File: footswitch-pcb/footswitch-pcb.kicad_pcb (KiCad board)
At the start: 2 copper layers, 56 x 22 mm, 18 parts, among them Q1 BUK7880-55A, U1 SeeeduinoXIAO

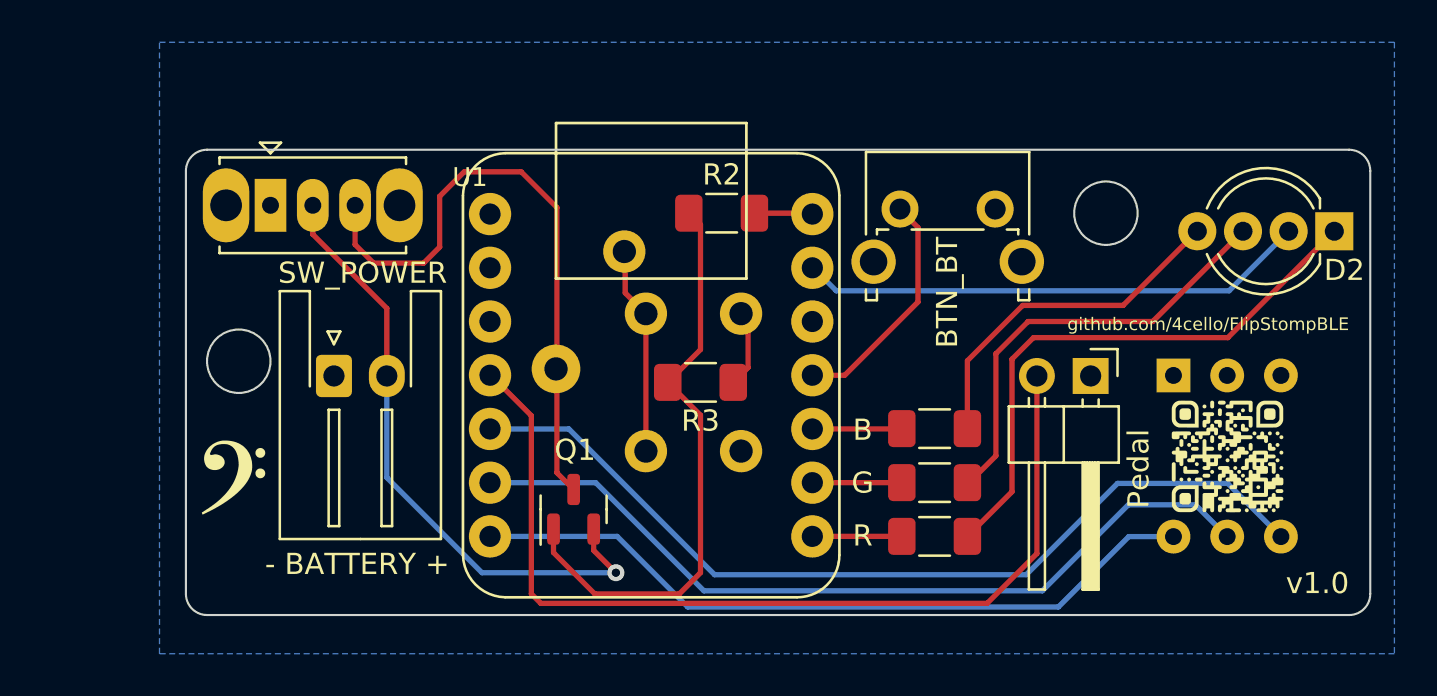
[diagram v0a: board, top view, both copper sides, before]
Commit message: Onboard Cherry Switch
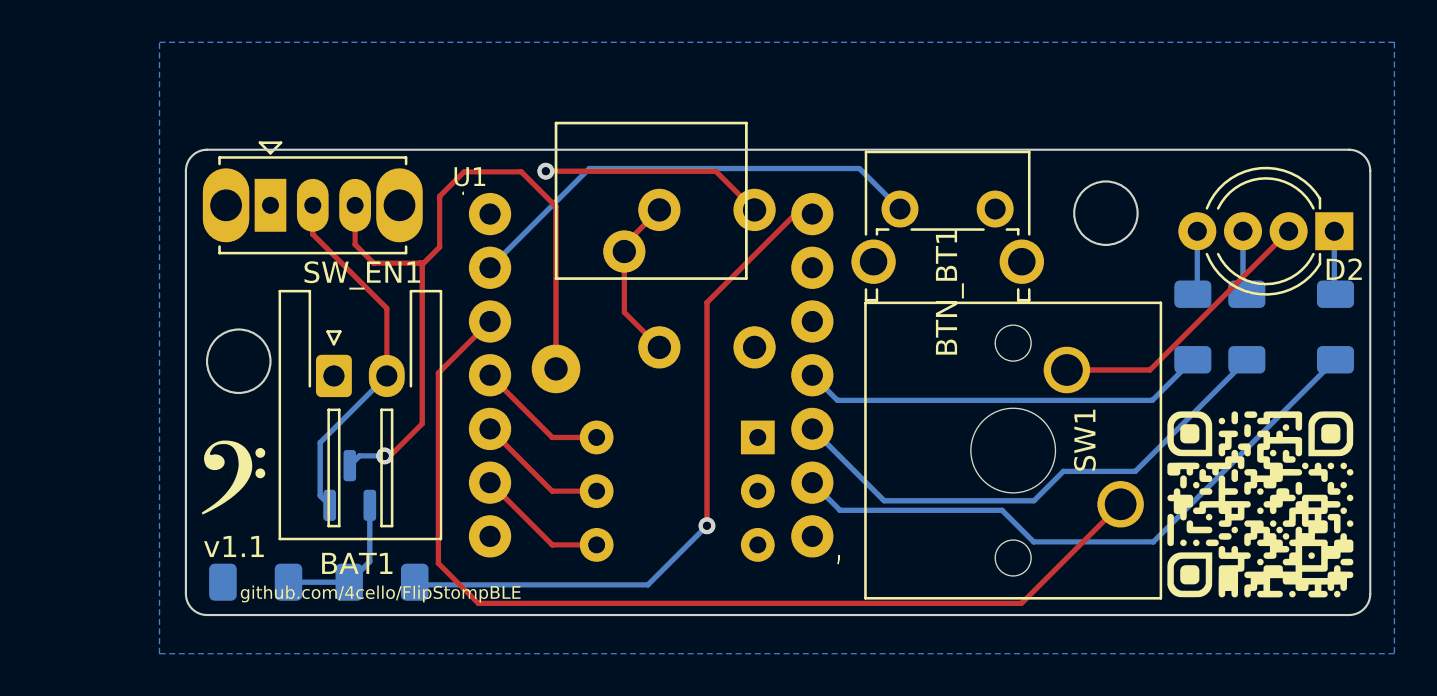
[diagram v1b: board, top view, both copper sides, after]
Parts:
- removed the G*** at (163.1, 85.6)
- removed the G*** at (149.8, 85.6)
- removed Pedal: Conn_Pedal, Connector_PinHeader_2.54mm:PinHeader_1x02_P2.54mm_Horizontal
- added SW1: SW_Push, Button_Switch_Keyboard:SW_Cherry_MX_1.00u_PCB, F.Cu at (158.0, 87.9)
- B1: renamed from B; moved to B.Cu
- BAT1: renamed from - BATTERY +
- G***: moved to F.Cu
- G1: renamed from G; moved to B.Cu
- Q1, R2, R3: moved to B.Cu
- R1: renamed from R; moved to B.Cu
- moved G*** 45.8 mm to (164.6, 87.9), turned to 0 degrees
- moved R2 23.7 mm to (123.1, 91.6)
- moved R3 23.1 mm to (117.2, 91.6), turned to 0 degrees
- moved R1 21.4 mm to (168.2, 79.5), turned to 90 degrees
- moved DIP_MODE1 19.9 mm to (140.9, 84.7), turned to 180 degrees
- moved G1 16.5 mm to (164.0, 79.5), turned to 90 degrees
- moved B1 13.1 mm to (161.5, 79.5), turned to -90 degrees
- moved Q1 10.6 mm to (121.6, 87.0)
- moved BTN_RESET1 4.95 mm to (136.2, 74.0)
- renumbered BTN_BT to BTN_BT1, BTN_RESET to BTN_RESET1, DIP_MODE to DIP_MODE1, SW_POWER to SW_EN1
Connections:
- U1 pad 10: PIN_LEDB -> PIN_LEDG
- U1 pad 11: PIN_BT -> PIN_LEDB
- U1 pad 2: unconnected-(U1-Pad2) -> PIN_BT
- U1 pad 3: unconnected-(U1-Pad3) -> PIN_PEDAL
- U1 pad 4: PIN_PEDAL -> PIN_LAYER3
- U1 pad 5: PIN_LAYER1 -> PIN_LAYER2
- U1 pad 6: PIN_LAYER2 -> PIN_LAYER1
- U1 pad 7: PIN_LAYER3 -> unconnected-(U1-Pad7)
- U1 pad 8: PIN_LEDR -> unconnected-(U1-Pad8)
- U1 pad 9: PIN_LEDG -> PIN_LEDR
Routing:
- net PIN_LAYER1: track 43.0 -> 6.26 mm
- net PIN_LAYER2: track 39.2 -> 6.26 mm
- net 5V_USB: track 2.80 -> 32.3 mm, vias 0 -> 1
- net PIN_LAYER3: track 35.0 -> 6.26 mm
- net PIN_LEDR: track 4.19 -> 29.5 mm
- net Net-(D2-Pad1): track 27.0 -> 3.00 mm
- net Net-(Q1-Pad1): track 27.8 -> 6.91 mm
- net PIN_LEDG: track 4.19 -> 24.7 mm
- net Net-(D2-Pad3): track 20.8 -> 3.05 mm
- net PIN_LEDB: track 4.19 -> 19.3 mm
- net Net-(B1-Pad1): track 16.6 -> 3.07 mm
- net Net-(BAT1-Pad2): track 29.5 -> 17.1 mm, vias 1 -> 0
- net PIN_BT: track 11.1 -> 22.1 mm
- net MCUBAT+: track 29.3 -> 35.2 mm, vias 0 -> 1
- net GND: track 27.6 -> 23.8 mm, vias 0 -> 1
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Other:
- board text added: "v1.1"

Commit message: Small cosmetic changes
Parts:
- turned R2 to 180 degrees
- turned R3 to 180 degrees
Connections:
- R2 pad 1: Net-(Q1-Pad1) -> 5V_USB
- R2 pad 2: 5V_USB -> Net-(Q1-Pad1)
- R3 pad 1: GND -> Net-(Q1-Pad1)
- R3 pad 2: Net-(Q1-Pad1) -> GND
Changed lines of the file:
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@@
     )
     (pad_to_mask_clearance 0)
-    (grid_origin 113.848 71.12)
+    (grid_origin 121.519 91.567)
     (pcbplotparams
       (layerselection 0x00010f0_ffffffff)
@@
   )
   (footprint "Resistor_SMD:R_1206_3216Metric_Pad1.30x1.75mm_HandSolder" (layer "B.Cu")
-    (at 117.15 91.567)
+    (at 117.15 91.567 180)
     (descr "Resistor SMD 1206 (3216 Metric), square (rectangular) end terminal, IPC_7351 nominal with elongated pad for handsoldering. (Body size source: IPC-SM-782 page 72, https://www.pcb-3d.com/wordpress/wp-content/uploads/ipc-sm-782a_amendment_1_and_2.pdf), generated with kicad-footprint-generator")
     (tags "resistor handsolder")
@@
     (fp_line (start -1.6 0.8) (end 1.6 0.8) (layer "B.Fab") (width 0.1))
     (fp_line (start -1.6 -0.8) (end -1.6 0.8) (layer "B.Fab") (width 0.1))
-    (pad "1" smd roundrect (at -1.55 0) (size 1.3 1.75) (layers "B.Cu" "B.Paste" "B.Mask") (roundrect_rratio 0.192308)
-      (net 1 "GND") (pintype "passive"))
-    (pad "2" smd roundrect (at 1.55 0) (size 1.3 1.75) (layers "B.Cu" "B.Paste" "B.Mask") (roundrect_rratio 0.192308)
+    (pad "1" smd roundrect (at -1.55 0 180) (size 1.3 1.75) (layers "B.Cu" "B.Paste" "B.Mask") (roundrect_rratio 0.192308)
       (net 14 "Net-(Q1-Pad1)") (pintype "passive"))
+    (pad "2" smd roundrect (at 1.55 0 180) (size 1.3 1.75) (layers "B.Cu" "B.Paste" "B.Mask") (roundrect_rratio 0.192308)
+      (net 1 "GND") (pintype "passive"))
     (model "${KICAD6_3DMODEL_DIR}/Resistor_SMD.3dshapes/R_1206_3216Metric.wrl"
       (offset (xyz 0 0 0))
@@
   )
   (footprint "Resistor_SMD:R_1206_3216Metric_Pad1.30x1.75mm_HandSolder" (layer "B.Cu")
-    (at 123.119 91.567)
+    (at 123.119 91.567 180)
     (descr "Resistor SMD 1206 (3216 Metric), square (rectangular) end terminal, IPC_7351 nominal with elongated pad for handsoldering. (Body size source: IPC-SM-782 page 72, https://www.pcb-3d.com/wordpress/wp-content/uploads/ipc-sm-782a_amendment_1_and_2.pdf), generated with kicad-footprint-generator")
     (tags "resistor handsolder")
@@
     (fp_line (start -1.6 0.8) (end 1.6 0.8) (layer "B.Fab") (width 0.1))
     (fp_line (start -1.6 -0.8) (end -1.6 0.8) (layer "B.Fab") (width 0.1))
-    (pad "1" smd roundrect (at -1.55 0) (size 1.3 1.75) (layers "B.Cu" "B.Paste" "B.Mask") (roundrect_rratio 0.192308)
-      (net 14 "Net-(Q1-Pad1)") (pintype "passive"))
-    (pad "2" smd roundrect (at 1.55 0) (size 1.3 1.75) (layers "B.Cu" "B.Paste" "B.Mask") (roundrect_rratio 0.192308)
+    (pad "1" smd roundrect (at -1.55 0 180) (size 1.3 1.75) (layers "B.Cu" "B.Paste" "B.Mask") (roundrect_rratio 0.192308)
       (net 16 "5V_USB") (pintype "passive"))
+    (pad "2" smd roundrect (at 1.55 0 180) (size 1.3 1.75) (layers "B.Cu" "B.Paste" "B.Mask") (roundrect_rratio 0.192308)
+      (net 14 "Net-(Q1-Pad1)") (pintype "passive"))
     (model "${KICAD6_3DMODEL_DIR}/Resistor_SMD.3dshapes/R_1206_3216Metric.wrl"
       (offset (xyz 0 0 0))
@@
   (segment (start 161.459485 77.952) (end 161.671 77.740485) (width 0.25) (layer "B.Cu") (net 13))
   (segment (start 161.671 77.740485) (end 161.671 74.974015) (width 0.25) (layer "B.Cu") (net 13))
-  (segment (start 121.569 91.567) (end 118.7 91.567) (width 0.25) (layer "B.Cu") (net 14))
+  (segment (start 118.7 91.567) (end 121.569 91.567) (width 0.25) (layer "B.Cu") (net 14))
   (segment (start 122.545 87.9325) (end 122.545 90.591) (width 0.25) (layer "B.Cu") (net 14))
   (segment (start 122.545 90.591) (end 121.569 91.567) (width 0.25) (layer "B.Cu") (net 14))
@@
   (segment (start 143.468 74.16203) (end 142.667113 74.16203) (width 0.25) (layer "F.Cu") (net 16))
   (via (at 138.486 88.9) (size 0.8) (drill 0.4) (layers "F.Cu" "B.Cu") (net 16))
-  (segment (start 124.796 91.694) (end 124.669 91.567) (width 0.25) (layer "B.Cu") (net 16))
-  (segment (start 135.692 91.694) (end 124.796 91.694) (width 0.25) (layer "B.Cu") (net 16))
-  (segment (start 138.486 88.9) (end 135.692 91.694) (width 0.25) (layer "B.Cu") (net 16))
+  (segment (start 135.819 91.567) (end 138.486 88.9) (width 0.25) (layer "B.Cu") (net 16))
+  (segment (start 124.669 91.567) (end 135.819 91.567) (width 0.25) (layer "B.Cu") (net 16))
   (segment (start 119.848 75.12) (end 119.848 73.747515) (width 0.25) (layer "F.Cu") (net 17))
   (segment (start 123.348 78.62) (end 119.848 75.12) (width 0.25) (layer "F.Cu") (net 17))

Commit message: Modified new PCB
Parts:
- removed B1, G1: R, Resistor_SMD:R_1206_3216Metric_Pad1.30x1.75mm_HandSolder
- removed BTN_BT1: BTN_BLUETOOTH, Button_Switch_THT:SW_Tactile_SPST_Angled_PTS645Vx39-2LFS
- removed BTN_RESET1: BTN_RESET, Button_Switch_THT:SW_PUSH_6mm_H7.3mm
- removed SW_EN1: SW_ENABLE, Button_Switch_THT:SW_Slide_1P2T_CK_OS102011MS2Q
- added BTN1: BT, Button_Switch_THT:SW_Tactile_SPST_Angled_PTS645Vx39-2LFS, F.Cu at (147.6, 73.9)
- added BTN2: RESET, Button_Switch_THT:SW_PUSH_6mm_H7.3mm, B.Cu at (136.2, 74.0)
- added R4: 10k, Resistor_SMD:R_1206_3216Metric_Pad1.30x1.75mm_HandSolder, B.Cu at (117.2, 91.6)
- added R5: 100, Resistor_SMD:R_1206_3216Metric_Pad1.30x1.75mm_HandSolder, B.Cu at (123.1, 91.6)
- added SW2: PWR, Button_Switch_THT:SW_Slide_1P2T_CK_OS102011MS2Q, F.Cu at (117.8, 73.7)
- R2: value 100 -> R
- R3: value 10k -> R
- SW1: value SW_Push -> PEDAL
- moved R3 45.9 mm to (161.5, 79.5), turned to -90 degrees
- moved R2 42.6 mm to (164.0, 79.5), turned to 90 degrees
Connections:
- D2 pad 4: Net-(B1-Pad1) -> Net-(R3-Pad1)
- R2 pad 1: 5V_USB -> PIN_LEDG
- R2 pad 2: Net-(Q1-Pad1) -> Net-(D2-Pad3)
- R3 pad 1: Net-(Q1-Pad1) -> Net-(R3-Pad1)
- R3 pad 2: GND -> PIN_LEDB
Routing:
- net Net-(R3-Pad1): track 0.00 -> 3.07 mm
- net Net-(B1-Pad1): track 3.07 -> 0.00 mm
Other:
- board text added: "${serialText}"
- board text added: "v${version}"
- board text removed: "v1.0"
- board text removed: "v1.1"
